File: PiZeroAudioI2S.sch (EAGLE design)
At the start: 69 parts, among them CON1 RPI-ZERO, J1 GROVE, J2 2X2HEADER, J3 2X1-LOCKING, J4 GROVE, J5 4X1-LOCKING, Q1 DMG2305UX, U1 TXB0104PWR, U2 LSM6DS33, U3 PCM5101A, U4 DMMT5401, U5 TXS0102, U6 TPA3144D2PWPR

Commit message: Added gnd to SCK pin
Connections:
- net GND: now also U3.SCK-12
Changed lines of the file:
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@@
 <wire x1="-276.86" y1="182.88" x2="-276.86" y2="190.5" width="0.1524" layer="91"/>
 <junction x="-276.86" y="190.5"/>
+<pinref part="U3" gate="G$1" pin="SCK-12"/>
+<wire x1="-276.86" y1="182.88" x2="-276.86" y2="177.8" width="0.1524" layer="91"/>
+<junction x="-276.86" y="182.88"/>
 </segment>
 <segment>

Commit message: Changed the name of RPI Header
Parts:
- CON1: value RPI-ZERO -> RPI-Header
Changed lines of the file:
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@@
 </classes>
 <parts>
-<part name="CON1" library="RPI-Zero" deviceset="RPI-ZERO" device=""/>
+<part name="CON1" library="RPI-Zero" deviceset="RPI-ZERO" device="" value="RPI-Header"/>
 <part name="P+3" library="supply1" library_urn="urn:adsk.eagle:library:371" deviceset="+5V" device=""/>
 <part name="+3V33" library="supply1" library_urn="urn:adsk.eagle:library:371" deviceset="+3V3" device=""/>

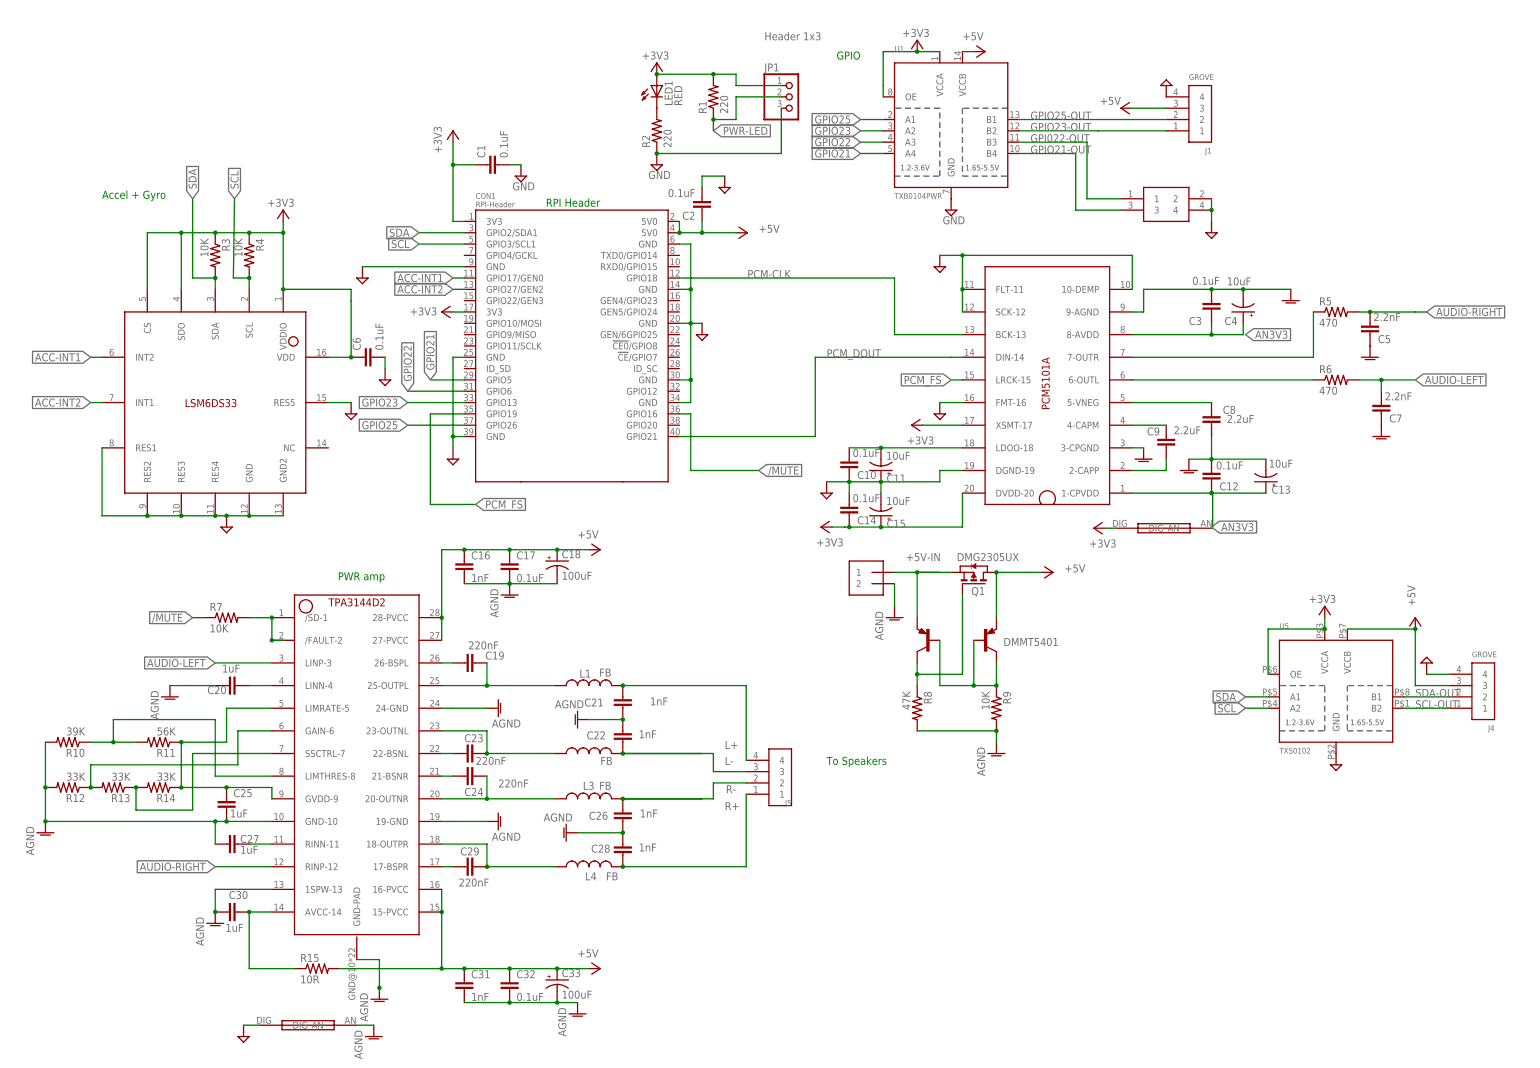
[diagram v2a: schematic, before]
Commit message: Swapped position of Mosfet Capacitively coupled Audio Set OE of I2C translator to GND Set Mute so it floats to +5
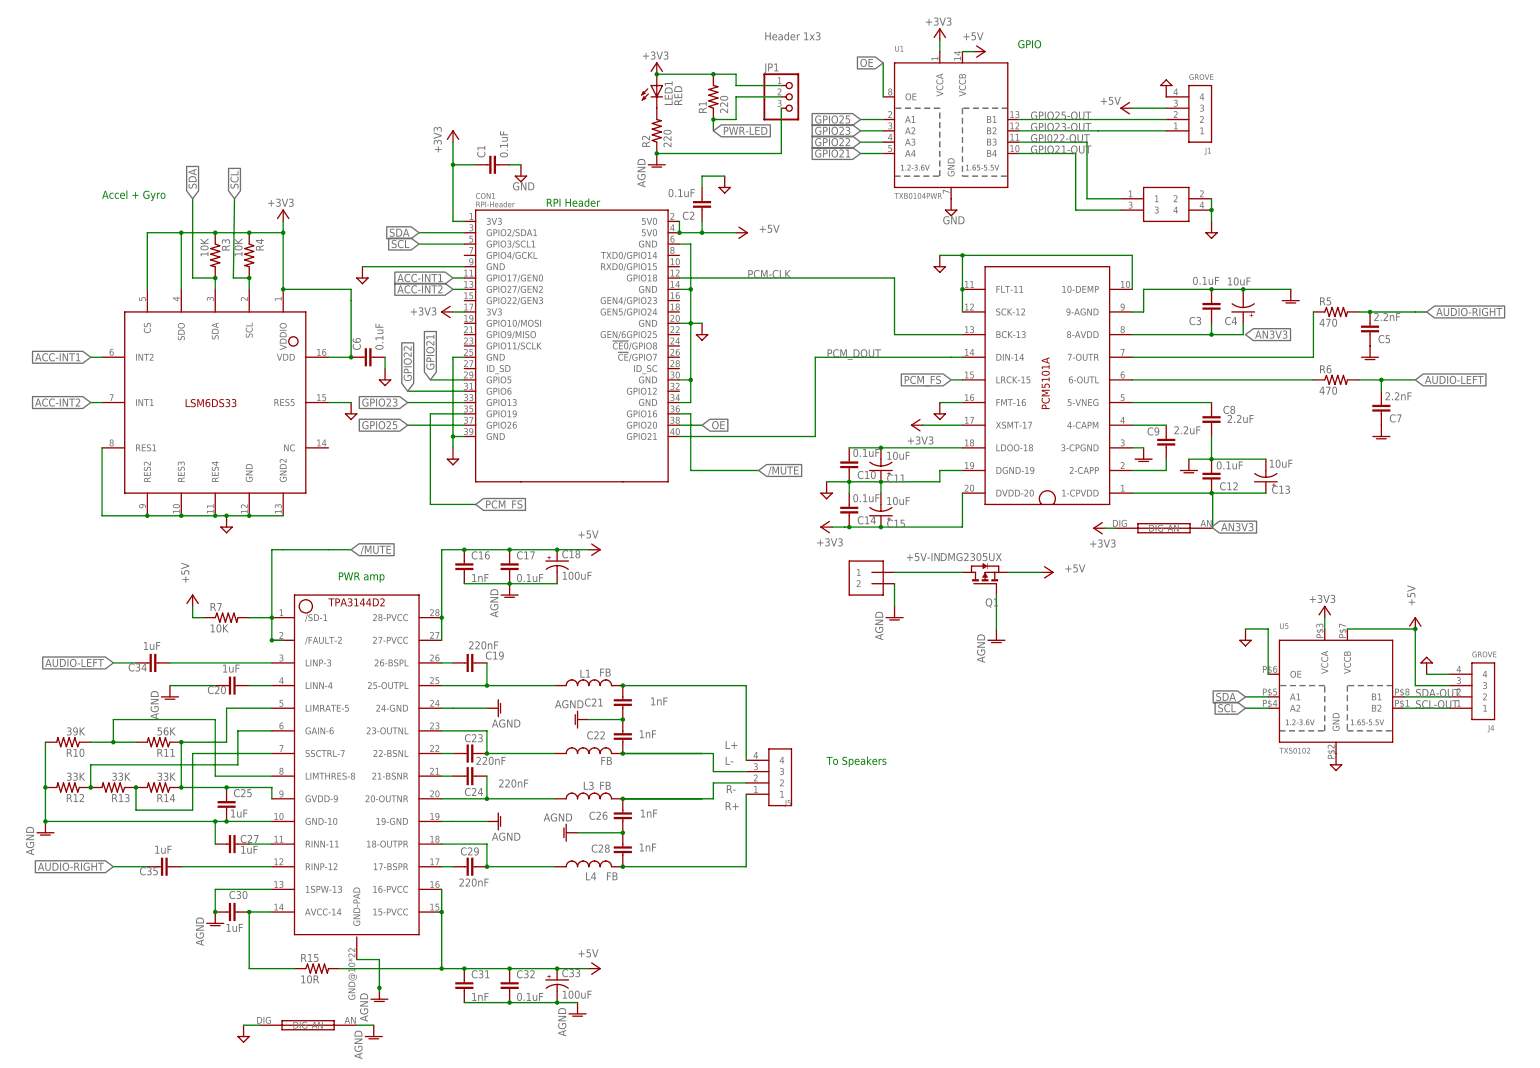
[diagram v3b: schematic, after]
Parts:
- removed R8: 47K, adafruit:R-US_R0603
- removed R9: 10K, adafruit:R-US_R0603
- removed U4: DMMT5401, HappyBrackets:DMMT5401
- added C34, C35: 1uF, rcl:C-EUC0603
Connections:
- removed net N$22: R9.1, U4G$1.B, U4G$2.B, U4G$2.C
- removed net N$27: Q1.G, R8.1, U4G$1.C
- removed net N$5: R7.2, U6./FAULT-2, U6./SD-1
- new net N$14: C34.1, U6.LINP-3
- new net N$15: C35.1, U6.RINP-12
- new net OE: CON1.GPIO20, U1.OE
- net +3V3: no longer U1.OE, U5.OE
- net +5V: now also Q1.S, R7.1; no longer Q1.D, U4G$2.E
- net +5V-IN: now also Q1.D; no longer Q1.S, U4G$1.E
- net /MUTE: now also R7.2, U6./FAULT-2, U6./SD-1; no longer R7.1
- net AGND: now also JP1.3, Q1.G, R2.1; no longer R8.2, R9.2
- net AUDIO-LEFT: now also C34.2; no longer U6.LINP-3
- net AUDIO-RIGHT: now also C35.2; no longer U6.RINP-12
- net GND: now also U5.OE; no longer JP1.3, R2.1
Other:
- moved on the sheet: Q1

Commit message: Build Revision 1
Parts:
- removed R14: 33K, adafruit:R-US_R0603
- removed R15: 10R, adafruit:R-US_R0603
- removed U6: TPA3144D2PWPR, HappyBrackets:TPA3144D2PWPR
- added R8: 39K, adafruit:R-US_R0603
- added R9: 56K, adafruit:R-US_R0603
- added U4: TXS0102, adafruit:TXS0102
- C1, C10, C12, C14, C17, C2, C3, C30, C6, CON1, J1, J2, J4, JP1, L1, L2, L3, L4, LED1, R1, R2, SH1, SH2: OC_FARNELL (none) -> unknown
- C11, C13, C15, C4: MF (none) -> AVX; MPN (none) -> F931C106MAA; OC_FARNELL (none) -> 2852673
- C16, C22: MF (none) -> AVX; MPN (none) -> 06035C102KAT2A; OC_FARNELL (none) -> 499134
- C18: MF (none) -> AVX; MPN (none) -> TLJA107M010R1400; OC_FARNELL (none) -> 2690441
- C19: value 220nF -> 1uF; OC_FARNELL (none) -> unknown
- C20, C25: value 1uF -> 220nF; MF (none) -> TAIYO YUDEN; MPN (none) -> EMK107B7224KA-T; OC_FARNELL (none) -> 1683648
- C21, C26, C28: value 1nF -> 1uF; OC_FARNELL (none) -> unknown
- C23, C29: value 220nF -> 1nF; MF (none) -> AVX; MPN (none) -> 06035C102KAT2A; OC_FARNELL (none) -> 499134
- C24: MF (none) -> TAIYO YUDEN; MPN (none) -> EMK107B7224KA-T; OC_FARNELL (none) -> 1683648
- C27: value 1uF -> 1nF; MF (none) -> AVX; MPN (none) -> 06035C102KAT2A; OC_FARNELL (none) -> 499134
- C31: value 1nF -> 220nF; MF (none) -> TAIYO YUDEN; MPN (none) -> EMK107B7224KA-T; OC_FARNELL (none) -> 1683648
- C32: value 0.1uF -> 1uF; OC_FARNELL (none) -> unknown
- C33: value 100uF -> 1nF; device HappyBrackets:CAP-POLARISED1206-POLAR -> rcl:C-EUC0603; MF (none) -> AVX; MPN (none) -> 06035C102KAT2A; OC_FARNELL (none) -> 499134
- C34: value 1uF -> 0.1uF; OC_FARNELL (none) -> unknown
- C35: value 1uF -> 100uF; device rcl:C-EUC0603 -> HappyBrackets:CAP-POLARISED1206-POLAR; MF (none) -> AVX; MPN (none) -> TLJA107M010R1400; OC_FARNELL (none) -> 2690441
- C5, C7: MF (none) -> WALSIN; MPN (none) -> 0603B222K500CT; OC_FARNELL (none) -> 2496845
- C8, C9: MF (none) -> KEMET; MPN (none) -> C0603C225K8PACTU; OC_FARNELL (none) -> 1108322
- J3: MF (none) -> MOLEX; MPN (none) -> 22-23-2021; OC_FARNELL (none) -> 1462926
- J5: MF (none) -> MOLEX; MPN (none) -> 22-23-2041; OC_FARNELL (none) -> 1462920
- Q1: MF (none) -> DIODES INC.; MPN (none) -> DMG2305UX-7; OC_FARNELL (none) -> 2543533
- R10: value 39K -> 33K; MF (none) -> MULTICOMP; MPN (none) -> MCMR06X3302FTL; OC_FARNELL (none) -> 2073473
- R11: value 56K -> 33K; MF (none) -> MULTICOMP; MPN (none) -> MCMR06X3302FTL; OC_FARNELL (none) -> 2073473
- R12: MF (none) -> MULTICOMP; MPN (none) -> MCMR06X3302FTL; OC_FARNELL (none) -> 2073473
- R13: value 33K -> 10R; OC_FARNELL (none) -> unknown
- R3, R4, R7: MF (none) -> YAGEO; MPN (none) -> RC0603FR-0710KL; OC_FARNELL (none) -> 2133286
- R5, R6: value 470 -> 80K; MF (none) -> PANASONIC ELECTRONIC COMPONENTS; MPN (none) -> ERJ3EKF4700V; OC_FARNELL (none) -> 2303120
- U1: MF (none) -> TEXAS INSTRUMENTS; MPN (none) -> TXB0104PWR; OC_FARNELL (none) -> 1607891
- U2: MF (none) -> STMICROELECTRONICS; MPN (none) -> LSM6DS33TR; OC_FARNELL (none) -> 2762756
- U3: MF (none) -> TEXAS INSTRUMENTS; MPN (none) -> PCM5101AQPWRQ1; OC_FARNELL (none) -> 2402250
- U5: value TXS0102 -> TPA3144D2PWPR; device adafruit:TXS0102 -> HappyBrackets:TPA3144D2PWPR; OC_FARNELL (none) -> unknown
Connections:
- net +3V3: now also U4.VCCA; no longer U5.VCCA
- net +5V: now also C33.1, C34.1, C35.+, R13.2, U4.VCCB, U5.15-PVCC, U5.16-PVCC, U5.27-PVCC, U5.28-PVCC; no longer C31.1, C32.1, C33.+, R15.2, U5.VCCB, U6.15-PVCC, U6.16-PVCC, U6.27-PVCC, U6.28-PVCC
- net /MUTE: now also U5./FAULT-2, U5./SD-1; no longer U6./FAULT-2, U6./SD-1
- net AGND: now also C22.2, C23.1, C28.2, C29.1, C33.2, C34.2, C35.-, R8.2, U5.19-GND, U5.1SPW-13, U5.24-GND, U5.GND-10, U5.GND-PAD; no longer C20.2, C22.1, C25.2, C28.1, C30.2, C31.2, C33.-, R12.2, U6.19-GND, U6.1SPW-13, U6.24-GND, U6.GND-10, U6.GND-PAD
- net AUDIO-LEFT: now also C19.2; no longer C34.2
- net AUDIO-RIGHT: now also C30.2; no longer C35.2
- net GND: now also U4.GND, U4.OE; no longer U5.GND, U5.OE
- net L+: now also C22.1; no longer C21.1
- net L-: now also C23.2; no longer C22.2
- net N$10: now also C31.2, U5.17-BSPR; no longer C29.2, U6.17-BSPR
- net N$13: now also C25.2, U5.21-BSNR; no longer C24.2, U6.21-BSNR
- net N$14: now also C19.1, U5.LINP-3; no longer C34.1, U6.LINP-3
- net N$15: now also C30.1, U5.RINP-12; no longer C35.1, U6.RINP-12
- net N$16: now also C24.2, U5.22-BSNL; no longer C23.2, U6.22-BSNL
- net N$17: now also C20.2, U5.26-BSPL; no longer C19.2, U6.26-BSPL
- net N$18: now also C20.1, U5.25-OUTPL; no longer C19.1, U6.25-OUTPL
- net N$19: now also C24.1, U5.23-OUTNL; no longer C23.1, U6.23-OUTNL
- net N$20: now also C25.1, U5.20-OUTNR; no longer C24.1, U6.20-OUTNR
- net N$21: now also C31.1, U5.18-OUTPR; no longer C29.1, U6.18-OUTPR
- net N$23: now also R10.1, R11.2, U5.GAIN-6; no longer R12.1, R13.2, U6.GAIN-6
- net N$24: now also R11.1, R12.2, U5.SSCTRL-7; no longer R13.1, R14.2, U6.SSCTRL-7
- net N$25: now also R8.1, R9.2, U5.LIMTHRES-8; no longer R10.1, R11.2, U6.LIMTHRES-8
- net N$26: now also C26.1, R12.1, R9.1, U5.GVDD-9, U5.LIMRATE-5; no longer C25.1, R11.1, R14.1, U6.GVDD-9, U6.LIMRATE-5
- net N$7: now also C21.1, U5.LINN-4; no longer C20.1, U6.LINN-4
- net N$8: now also C28.1, U5.RINN-11; no longer C27.1, U6.RINN-11
- net N$9: now also C32.1, R13.1, U5.AVCC-14; no longer C30.1, R15.1, U6.AVCC-14
- net R+: now also C29.2; no longer C28.2
- net R-: now also C27.1; no longer C26.1
- net SCL: now also U4.A2; no longer U5.A2
- net SCL-OUT: now also U4.B2; no longer U5.B2
- net SDA: now also U4.A1; no longer U5.A1
- net SDA-OUT: now also U4.B1; no longer U5.B1
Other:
- moved on the sheet: C19, C20, C21, C22, C23, C24, C25, C26, C27, C28, C29, C30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

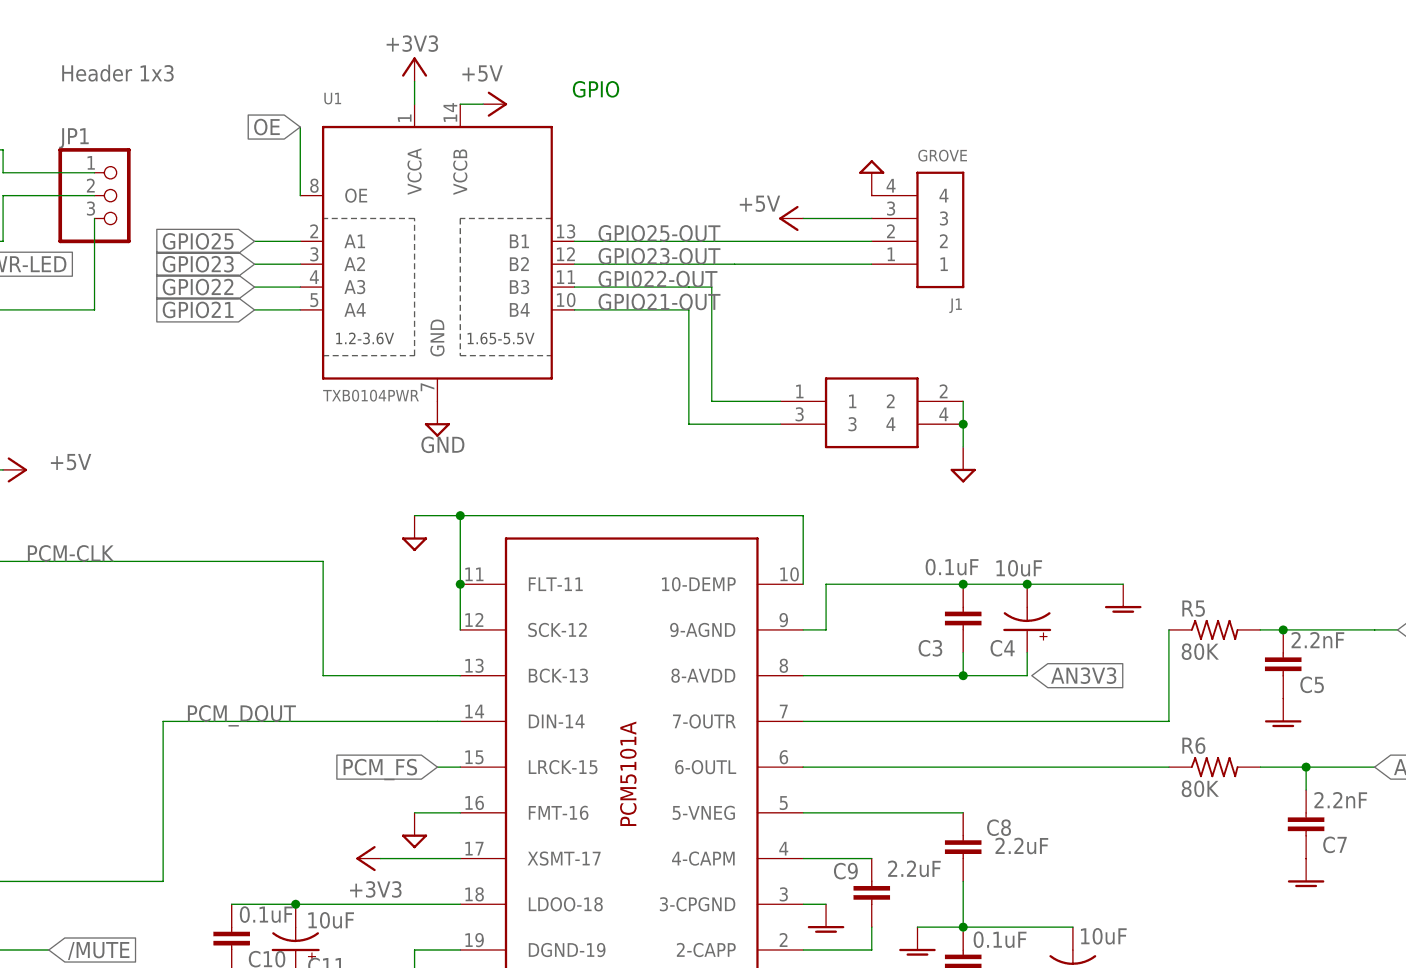
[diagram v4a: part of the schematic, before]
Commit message: Added R14 10K resistance to translator
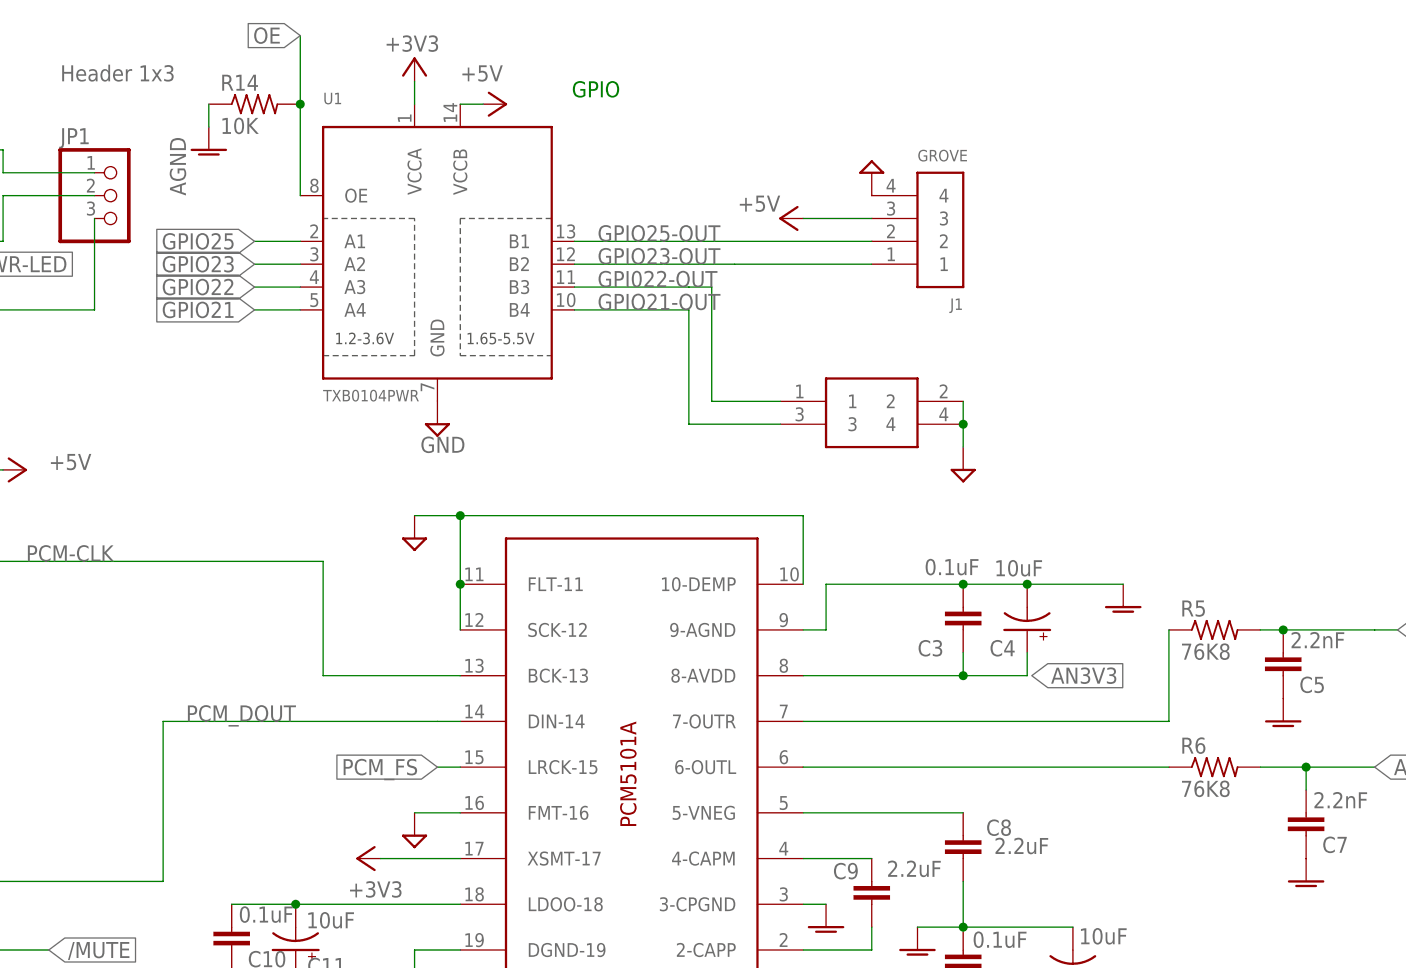
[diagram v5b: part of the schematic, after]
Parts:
- added R14: 10K, adafruit:R-US_R0603
- R5, R6: value 80K -> 76K8
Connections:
- net AGND: now also R14.1
- net OE: now also R14.2
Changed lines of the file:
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@@
 <attribute name="OC_FARNELL" value="2496845"/>
 </part>
-<part name="R5" library="adafruit" deviceset="R-US_" device="R0603" value="80K">
+<part name="R5" library="adafruit" deviceset="R-US_" device="R0603" value="76K8">
 <attribute name="MF" value="PANASONIC ELECTRONIC COMPONENTS"/>
 <attribute name="MPN" value="ERJ3EKF4700V"/>
 <attribute name="OC_FARNELL" value="2303120"/>
 </part>
-<part name="R6" library="adafruit" deviceset="R-US_" device="R0603" value="80K">
+<part name="R6" library="adafruit" deviceset="R-US_" device="R0603" value="76K8">
 <attribute name="MF" value="PANASONIC ELECTRONIC COMPONENTS"/>
 <attribute name="MPN" value="ERJ3EKF4700V"/>
@@
 <part name="P+6" library="supply1" library_urn="urn:adsk.eagle:library:371" deviceset="+5V" device=""/>
 <part name="AGND1" library="supply1" library_urn="urn:adsk.eagle:library:371" deviceset="AGND" device=""/>
+<part name="R14" library="adafruit" deviceset="R-US_" device="R0603" value="10K">
+<attribute name="MF" value="YAGEO"/>
+<attribute name="MPN" value="RC0603FR-0710KL"/>
+<attribute name="OC_FARNELL" value="2133286"/>
+</part>
+<part name="AGND20" library="supply1" library_urn="urn:adsk.eagle:library:371" deviceset="AGND" device=""/>
 </parts>
 <sheets>
@@
 </instance>
 <instance part="AGND1" gate="VR1" x="-345.44" y="210.82"/>
+<instance part="R14" gate="G$1" x="-299.72" y="236.22">
+<attribute name="OC_FARNELL" x="-299.72" y="236.22" size="1.778" layer="96" rot="R90" display="off"/>
+<attribute name="MF" x="-299.72" y="236.22" size="1.778" layer="96" rot="R90" display="off"/>
+<attribute name="MPN" x="-299.72" y="236.22" size="1.778" layer="96" rot="R90" display="off"/>
+</instance>
+<instance part="AGND20" gate="VR1" x="-304.8" y="231.14"/>
 </instances>
 <busses>
@@
 <junction x="-345.44" y="213.36"/>
 </segment>
+<segment>
+<pinref part="R14" gate="G$1" pin="1"/>
+<wire x1="-304.8" y1="233.68" x2="-304.8" y2="236.22" width="0.1524" layer="91"/>
+<pinref part="AGND20" gate="VR1" pin="AGND"/>
+</segment>
 </net>
 <net name="AUDIO-LEFT" class="0">
@@
 <segment>
 <pinref part="U1" gate="G$1" pin="OE"/>
-<wire x1="-294.64" y1="233.68" x2="-294.64" y2="226.06" width="0.1524" layer="91"/>
-<label x="-294.64" y="233.68" size="1.778" layer="95" rot="R180" xref="yes"/>
-</segment>
-</net>
+<wire x1="-294.64" y1="243.84" x2="-294.64" y2="236.22" width="0.1524" layer="91"/>
+<label x="-294.64" y="243.84" size="1.778" layer="95" rot="R180" xref="yes"/>
+<pinref part="R14" gate="G$1" pin="2"/>
+<wire x1="-294.64" y1="236.22" x2="-294.64" y2="226.06" width="0.1524" layer="91"/>
+<junction x="-294.64" y="236.22"/>
+</segment>
+</net>
